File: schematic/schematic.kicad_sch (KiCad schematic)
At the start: 1 part

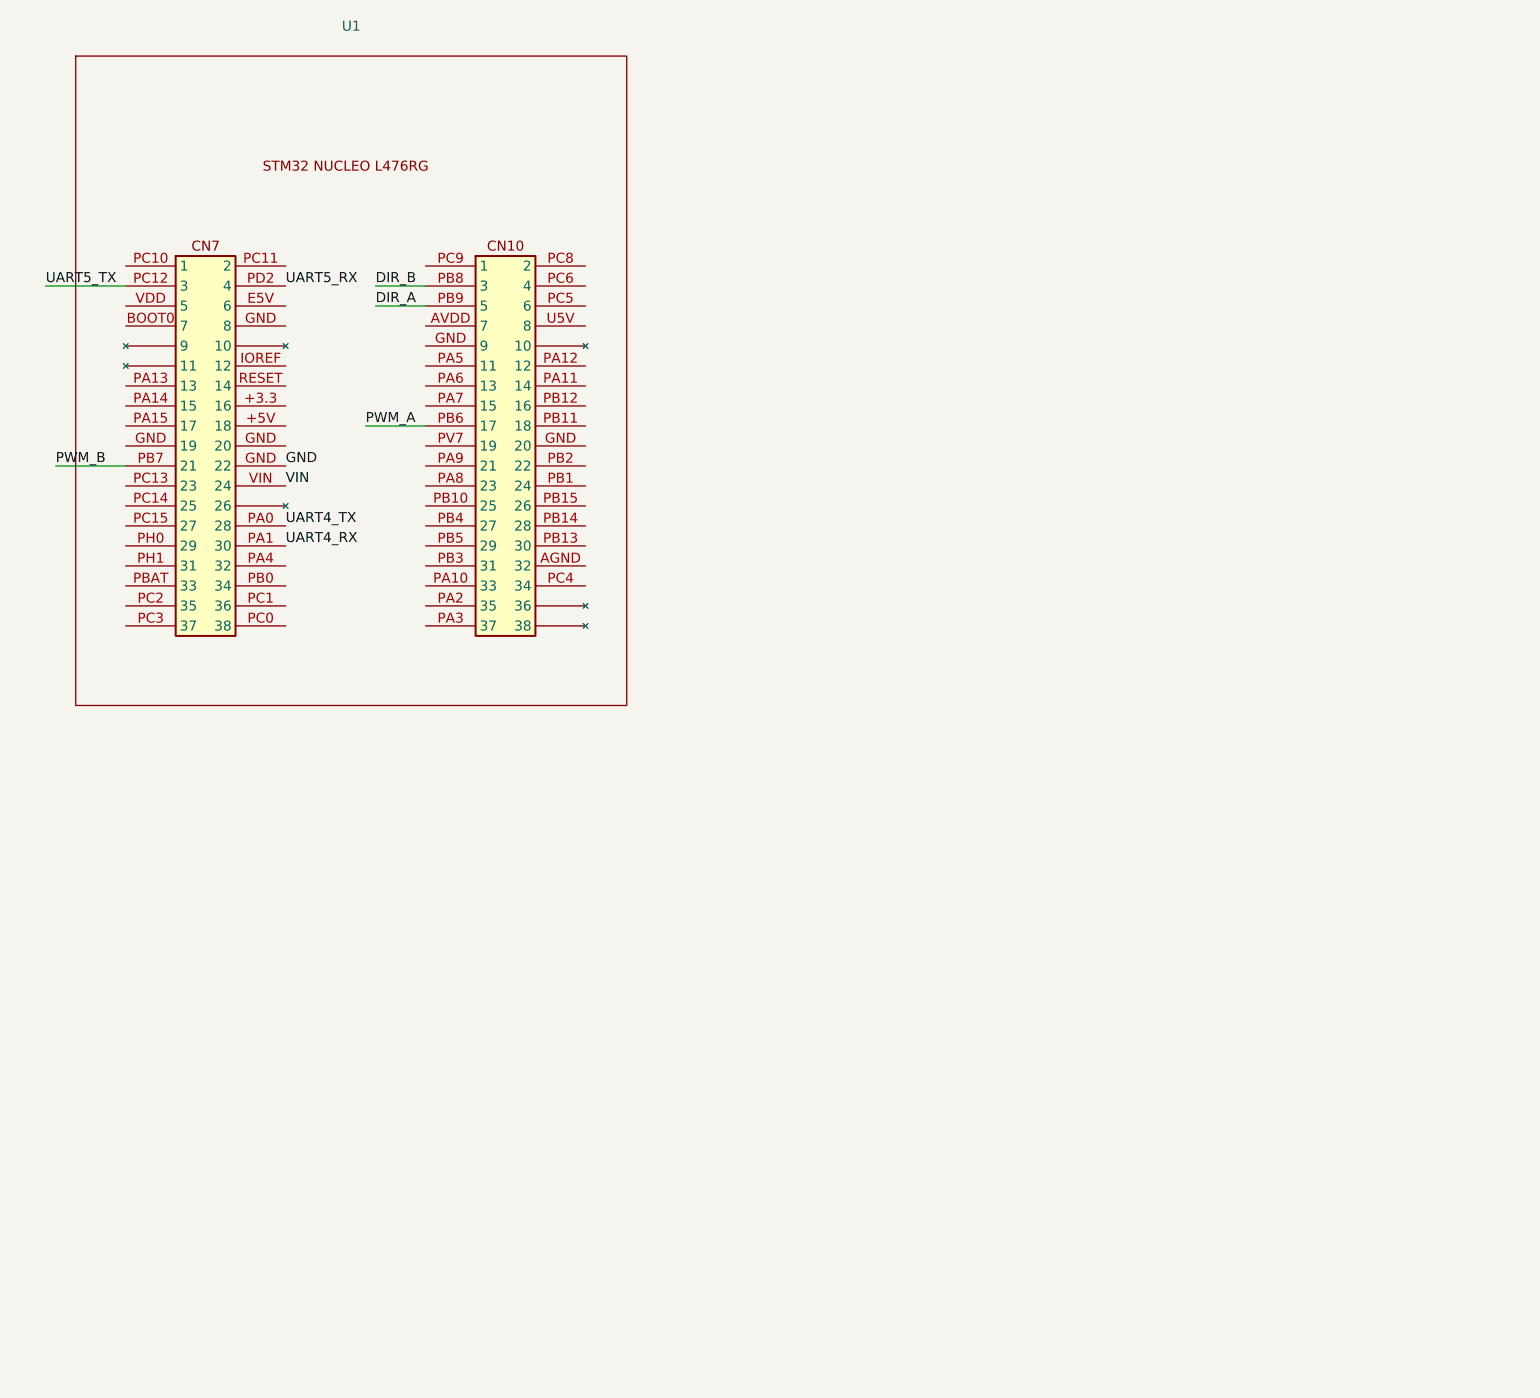
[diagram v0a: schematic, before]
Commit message: Updated schematic and added blinkey status lights
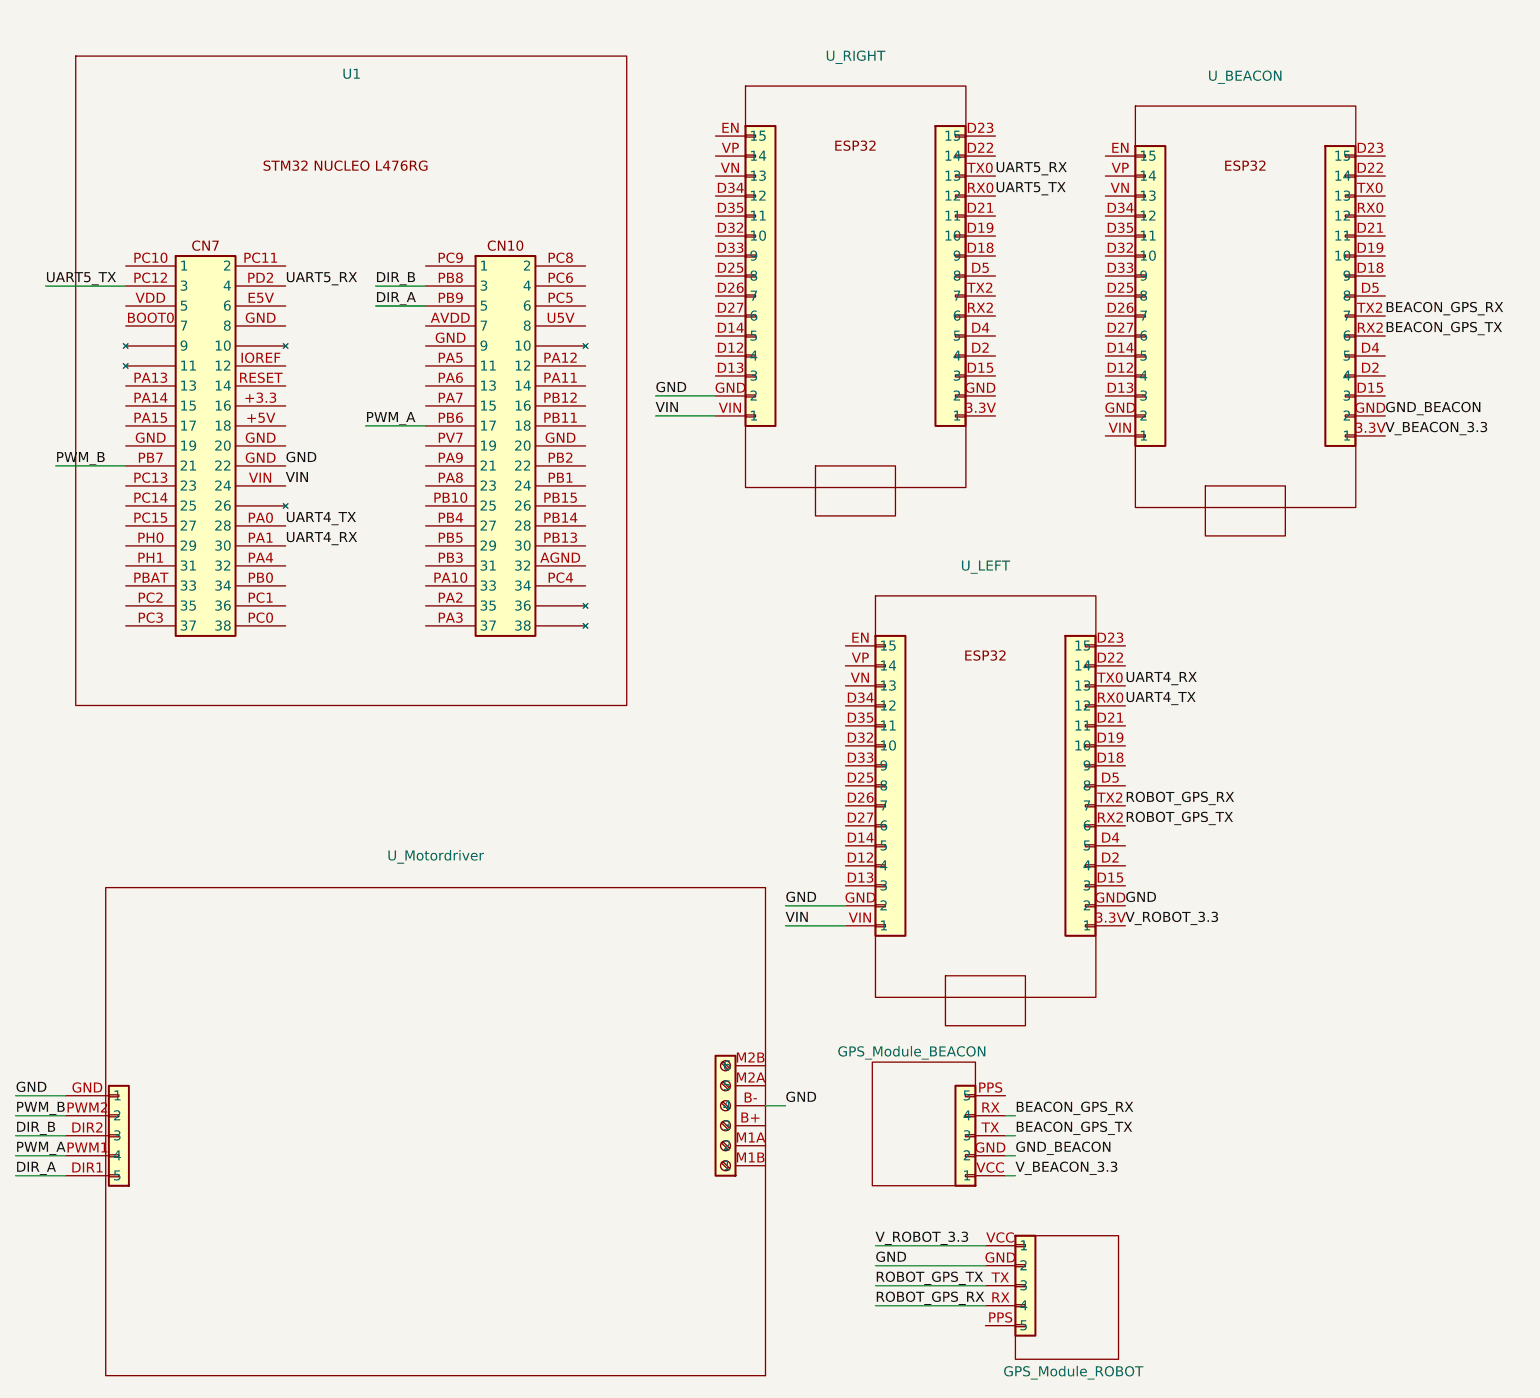
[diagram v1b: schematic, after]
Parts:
- added GPS_Module_BEACON, GPS_Module_ROBOT: ~, symbol school_projects:GPS_Module
- added U_BEACON, U_LEFT, U_RIGHT: ~, symbol school_projects:ESP32
- added U_Motordriver: ~, symbol school_projects:Motor_driver
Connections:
- net DIR_A: now also U_Motordriver.DIR1 (5)
- net DIR_B: now also U_Motordriver.DIR2 (3)
- net GND: now also GPS_Module_ROBOT.GND (2), U_LEFT.GND (2), U_Motordriver.B- (4), U_Motordriver.GND (1), U_RIGHT.GND (2)
- net PWM_A: now also U_Motordriver.PWM1 (4)
- net PWM_B: now also U_Motordriver.PWM2 (2)
- net UART4_RX: now also U_LEFT.TX0 (13)
- net UART4_TX: now also U_LEFT.RX0 (12)
- net UART5_RX: now also U_RIGHT.TX0 (13)
- net UART5_TX: now also U_RIGHT.RX0 (12)
- net VIN: now also U_LEFT.VIN (1), U_RIGHT.VIN (1)
- new net BEACON_GPS_RX: GPS_Module_BEACON.RX (4), U_BEACON.TX2 (7)
- new net BEACON_GPS_TX: GPS_Module_BEACON.TX (3), U_BEACON.RX2 (6)
- new net GND_BEACON: GPS_Module_BEACON.GND (2), U_BEACON.GND (2)
- new net ROBOT_GPS_RX: GPS_Module_ROBOT.RX (4), U_LEFT.TX2 (7)
- new net ROBOT_GPS_TX: GPS_Module_ROBOT.TX (3), U_LEFT.RX2 (6)
- new net V_BEACON_3.3: GPS_Module_BEACON.VCC (1), U_BEACON.3.3V (1)
- new net V_ROBOT_3.3: GPS_Module_ROBOT.VCC (1), U_LEFT.3.3V (1)
